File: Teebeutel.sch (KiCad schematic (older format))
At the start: 66 parts, among them J1 RJ45_Shielded, J2 Conn_01x30_Female, J3 Micro_SD_Card, Q1 S8050, Q2 S8050, SW1 K1-1506SN-01, U1 ESP32-WROOM-32, U2 TLV1117-33, U3 MCP73831-2-OT, U4 SDB628, U5 LIS2DE12, U6 TLV70018_SOT23-5, U7 SGP30, U8 PPSI262, U9 TXB0104RUT

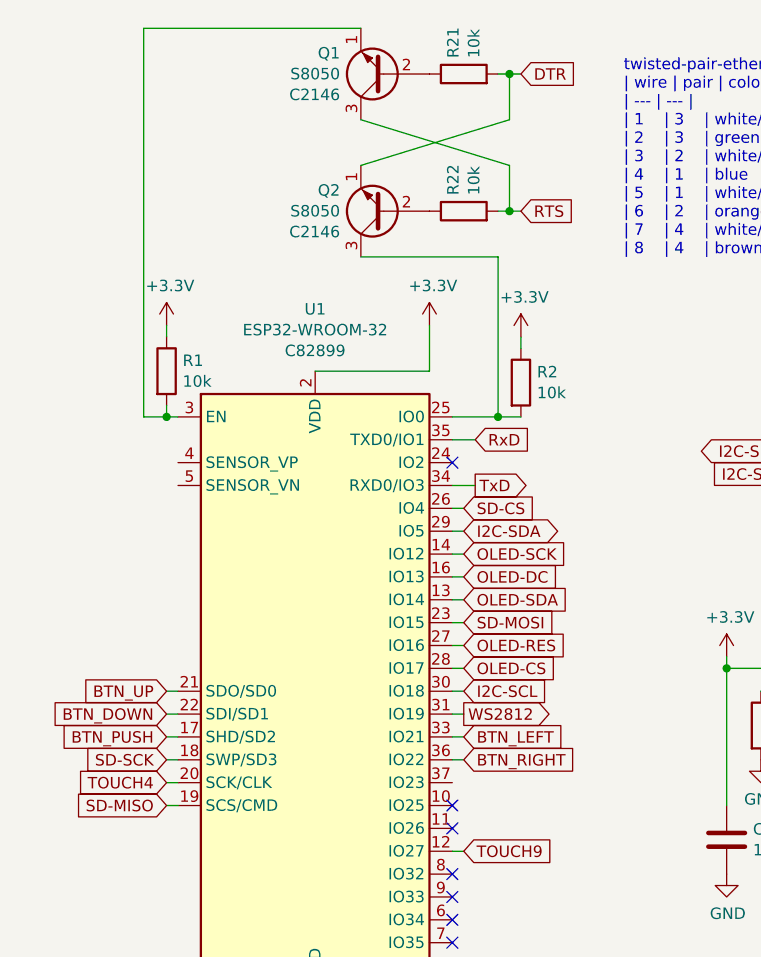
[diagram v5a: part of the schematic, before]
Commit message: fix: Move pulldown R in the Boot-mode selector
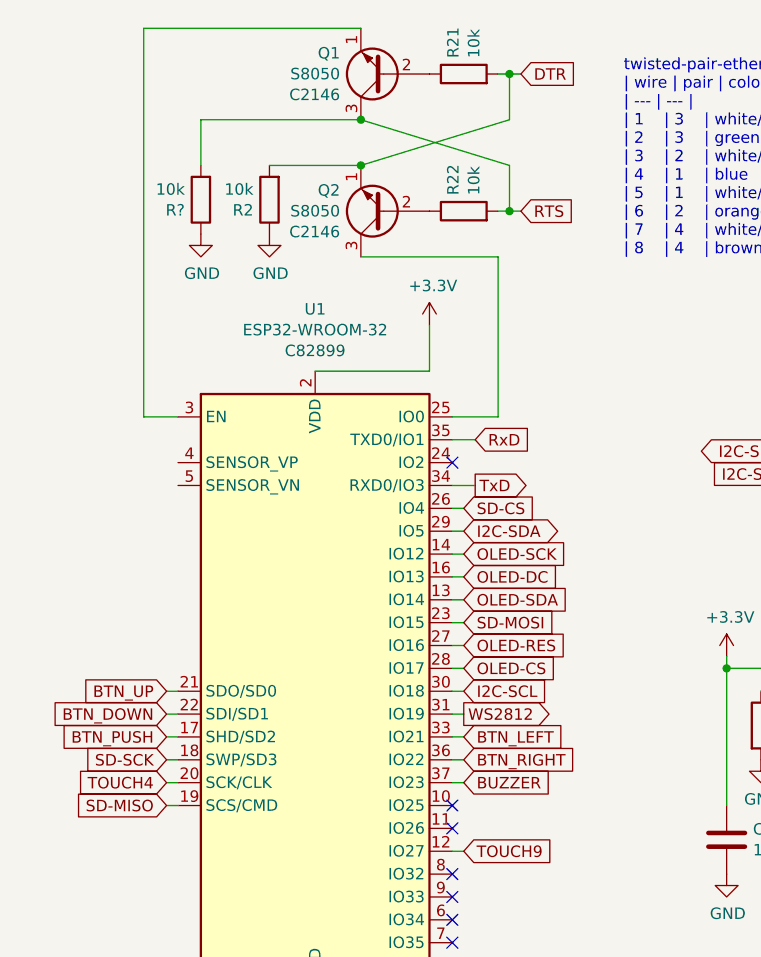
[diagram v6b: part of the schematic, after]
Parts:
- removed R1: 10k, Resistor_SMD:R_0603_1608Metric, symbol Device:R
- added R?: 10k, Resistor_SMD:R_0603_1608Metric, symbol Device:R
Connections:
- net +3V3: no longer R2.1
- net DTR: now also R2.2
- net GND: now also R2.1, R?.1
- net RTS: now also R?.2
- net at Q2.3 (C), U1.25 (IO0): no longer R2.2
- net BUZZER: now reaches U1.37 (IO23)
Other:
- moved on the sheet: R2
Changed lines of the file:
@@
 Wire Wire Line
 	2300 2500 2400 2500
-Wire Wire Line
-	1100 2200 1050 2200
 $Comp
 L power:GND #PWR0106
@@
 $EndComp
 Wire Wire Line
-	2600 1900 2600 1850
-$Comp
-L power:+3.3V #PWR0107
-U 1 1 6189001F
-P 2600 1850
-F 0 "#PWR0107" H 2600 1700 50  0001 C CNN
-F 1 "+3.3V" H 2615 2023 50  0000 C CNN
-F 2 "" H 2600 1850 50  0001 C CNN
-F 3 "" H 2600 1850 50  0001 C CNN
-	1    2600 1850
-	1    0    0    -1
-$EndComp
-Wire Wire Line
 	2300 2200 2500 2200
-Connection ~ 2500 2200
 $Comp
 L Device:R R2
 U 1 1 6188F20B
-P 2600 2050
-F 0 "R2" H 2670 2096 50  0000 L CNN
-F 1 "10k" H 2670 2005 50  0000 L CNN
-F 2 "Resistor_SMD:R_0603_1608Metric" V 2530 2050 50  0001 C CNN
-F 3 "~" H 2600 2050 50  0001 C CNN
-	1    2600 2050
-	1    0    0    -1
-$EndComp
-$Comp
-L Device:R R1
-U 1 1 618931A3
-P 1050 2000
-F 0 "R1" H 1120 2046 50  0000 L CNN
-F 1 "10k" H 1120 1955 50  0000 L CNN
-F 2 "Resistor_SMD:R_0603_1608Metric" V 980 2000 50  0001 C CNN
-F 3 "~" H 1050 2000 50  0001 C CNN
-	1    1050 2000
-	1    0    0    -1
-$EndComp
-Wire Wire Line
-	1050 2200 1050 2150
-$Comp
-L power:+3.3V #PWR0108
-U 1 1 618931AA
-P 1050 1800
-F 0 "#PWR0108" H 1050 1650 50  0001 C CNN
-F 1 "+3.3V" H 1065 1973 50  0000 C CNN
-F 2 "" H 1050 1800 50  0001 C CNN
-F 3 "" H 1050 1800 50  0001 C CNN
-	1    1050 1800
-	1    0    0    -1
-$EndComp
-Wire Wire Line
-	1050 1850 1050 1800
-Wire Wire Line
-	950  2200 1050 2200
-Connection ~ 1050 2200
-Wire Wire Line
-	2500 2200 2600 2200
+P 1500 1250
+F 0 "R2" H 1570 1296 50  0000 L CNN
+F 1 "10k" H 1570 1205 50  0000 L CNN
+F 2 "Resistor_SMD:R_0603_1608Metric" V 1430 1250 50  0001 C CNN
+F 3 "~" H 1500 1250 50  0001 C CNN
+	1    1500 1250
+	-1   0    0    1
+$EndComp
 NoConn ~ 2300 2400
 Wire Wire Line
@@
 Wire Wire Line
 	950  500  1900 500
+Wire Wire Line
+	950  2200 1100 2200
+$Comp
+L power:GND #PWR?
+U 1 1 61873CA9
+P 1500 1400
+F 0 "#PWR?" H 1500 1150 50  0001 C CNN
+F 1 "GND" H 1505 1227 50  0000 C CNN
+F 2 "" H 1500 1400 50  0001 C CNN
+F 3 "" H 1500 1400 50  0001 C CNN
+	1    1500 1400
+	1    0    0    -1
+$EndComp
+$Comp
+L Device:R R?
+U 1 1 6187475E
+P 1200 1250
+F 0 "R?" H 1270 1296 50  0000 L CNN
+F 1 "10k" H 1270 1205 50  0000 L CNN
+F 2 "Resistor_SMD:R_0603_1608Metric" V 1130 1250 50  0001 C CNN
+F 3 "~" H 1200 1250 50  0001 C CNN
+	1    1200 1250
+	-1   0    0    1
+$EndComp
+$Comp
+L power:GND #PWR?
+U 1 1 61874765
+P 1200 1400
+F 0 "#PWR?" H 1200 1150 50  0001 C CNN
+F 1 "GND" H 1205 1227 50  0000 C CNN
+F 2 "" H 1200 1400 50  0001 C CNN
+F 3 "" H 1200 1400 50  0001 C CNN
+	1    1200 1400
+	1    0    0    -1
+$EndComp
+Wire Wire Line
+	1200 900  1200 1100
+Wire Wire Line
+	1200 900  1900 900
+Connection ~ 1900 900
+Wire Wire Line
+	1500 1100 1900 1100
+Connection ~ 1900 1100
+Text GLabel 2350 3800 2    50   Input ~ 0
+BUZZER
+Wire Wire Line
+	2350 3800 2300 3800
 $EndSCHEMATC

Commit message: feat: add buzzer
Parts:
- added BZ1: Buzzer, symbol Device:Buzzer
- added D10: SM4007, Diode_SMD:D_SOD-123, symbol Diode:SM4007
- added Q3: S8050, Package_TO_SOT_THT:TO-92_Inline, symbol Transistor_BJT:S8050
- added R23: 180, Resistor_SMD:R_0603_1608Metric, symbol Device:R
- gave numbers to parts that had none: 1
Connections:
- wire segments 224 -> 228
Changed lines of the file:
@@
 	950  2200 1100 2200
 $Comp
-L power:GND #PWR?
+L power:GND #PWR0107
 U 1 1 61873CA9
 P 1500 1400
-F 0 "#PWR?" H 1500 1150 50  0001 C CNN
+F 0 "#PWR0107" H 1500 1150 50  0001 C CNN
 F 1 "GND" H 1505 1227 50  0000 C CNN
 F 2 "" H 1500 1400 50  0001 C CNN
@@
 $EndComp
 $Comp
-L Device:R R?
+L Device:R R1
 U 1 1 6187475E
 P 1200 1250
-F 0 "R?" H 1270 1296 50  0000 L CNN
+F 0 "R1" H 1270 1296 50  0000 L CNN
 F 1 "10k" H 1270 1205 50  0000 L CNN
 F 2 "Resistor_SMD:R_0603_1608Metric" V 1130 1250 50  0001 C CNN
@@
 $EndComp
 $Comp
-L power:GND #PWR?
+L power:GND #PWR0108
 U 1 1 61874765
 P 1200 1400
-F 0 "#PWR?" H 1200 1150 50  0001 C CNN
+F 0 "#PWR0108" H 1200 1150 50  0001 C CNN
 F 1 "GND" H 1205 1227 50  0000 C CNN
 F 2 "" H 1200 1400 50  0001 C CNN
@@
 Wire Wire Line
 	2350 3800 2300 3800
+$Comp
+L Device:Buzzer BZ1
+U 1 1 61862B5F
+P 5900 4350
+F 0 "BZ1" H 6052 4424 50  0000 L CNN
+F 1 "Buzzer" H 6052 4333 50  0000 L CNN
+F 2 "" V 5875 4450 50  0001 C CNN
+F 3 "https://datasheet.lcsc.com/lcsc/2005191833_KELIKING-KLJ-5020_C556937.pdf" V 5875 4450 50  0001 C CNN
+F 4 "C556937" H 6052 4242 50  0000 L CNN "JLCPCB"
+	1    5900 4350
+	1    0    0    -1
+$EndComp
+Text GLabel 5200 4650 0    50   Input ~ 0
+BUZZER
+$Comp
+L power:GND #PWR0184
+U 1 1 61863E23
+P 5800 4850
+F 0 "#PWR0184" H 5800 4600 50  0001 C CNN
+F 1 "GND" H 5805 4677 50  0000 C CNN
+F 2 "" H 5800 4850 50  0001 C CNN
+F 3 "" H 5800 4850 50  0001 C CNN
+	1    5800 4850
+	1    0    0    -1
+$EndComp
+$Comp
+L Transistor_BJT:S8050 Q3
+U 1 1 61867FEB
+P 5700 4650
+F 0 "Q3" H 5890 4741 50  0000 L CNN
+F 1 "S8050" H 5890 4650 50  0000 L CNN
+F 2 "Package_TO_SOT_THT:TO-92_Inline" H 5900 4575 50  0001 L CIN
+F 3 "http://www.unisonic.com.tw/datasheet/S8050.pdf" H 5700 4650 50  0001 L CNN
+F 4 "C2146" H 5890 4559 50  0000 L CNN "JLCPCB"
+	1    5700 4650
+	1    0    0    -1
+$EndComp
+$Comp
+L Device:R R23
+U 1 1 6186A578
+P 5350 4650
+F 0 "R23" H 5420 4696 50  0000 L CNN
+F 1 "180" H 5420 4605 50  0000 L CNN
+F 2 "Resistor_SMD:R_0603_1608Metric" V 5280 4650 50  0001 C CNN
+F 3 "~" H 5350 4650 50  0001 C CNN
+	1    5350 4650
+	0    -1   -1   0
+$EndComp
+Connection ~ 5800 4450
+Wire Wire Line
+	5800 4150 5800 4250
+$Comp
+L power:+3.3V #PWR0185
+U 1 1 619097C0
+P 5700 4150
+F 0 "#PWR0185" H 5700 4000 50  0001 C CNN
+F 1 "+3.3V" H 5715 4323 50  0000 C CNN
+F 2 "" H 5700 4150 50  0001 C CNN
+F 3 "" H 5700 4150 50  0001 C CNN
+	1    5700 4150
+	1    0    0    -1
+$EndComp
+Connection ~ 5700 4150
+Wire Wire Line
+	5700 4150 5800 4150
+$Comp
+L Diode:SM4007 D10
+U 1 1 6190B41E
+P 5450 4300
+F 0 "D10" V 5359 4380 50  0000 L CNN
+F 1 "SM4007" V 5450 4380 50  0000 L CNN
+F 2 "Diode_SMD:D_SOD-123" H 5450 4125 50  0001 C CNN
+F 3 "http://cdn-reichelt.de/documents/datenblatt/A400/SMD1N400%23DIO.pdf" H 5450 4300 50  0001 C CNN
+F 4 "C64898" V 5541 4380 50  0000 L CNN "JLCPCB"
+	1    5450 4300
+	0    1    1    0
+$EndComp
+Wire Wire Line
+	5450 4150 5700 4150
+Wire Wire Line
+	5450 4450 5800 4450
 $EndSCHEMATC

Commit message: feat: add llc for uart
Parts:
- added U?: TXB0104RUT, Package_DFN_QFN:Texas_R_PUQFN-N12, symbol Logic_LevelTranslator:TXB0104RUT
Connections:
- wire segments 228 -> 238
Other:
- moved on the sheet: C18, C19, J3, Q3, R16, R17, R18, R19, R20, R23, U8
